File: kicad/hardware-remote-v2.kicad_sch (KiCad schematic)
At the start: 25 parts, among them J1 Flash, J2 TFT, J3 5VIN, J4 3.3VIN, J5 Conn_02x08_Odd_Even, Q1 SI2301CDS-T1-GE3, SW1 ANALOG_LEFT, SW2 ANALOG_RIGHT, U1 ESP32-WROOM-32, U2 AMS1117-3.3

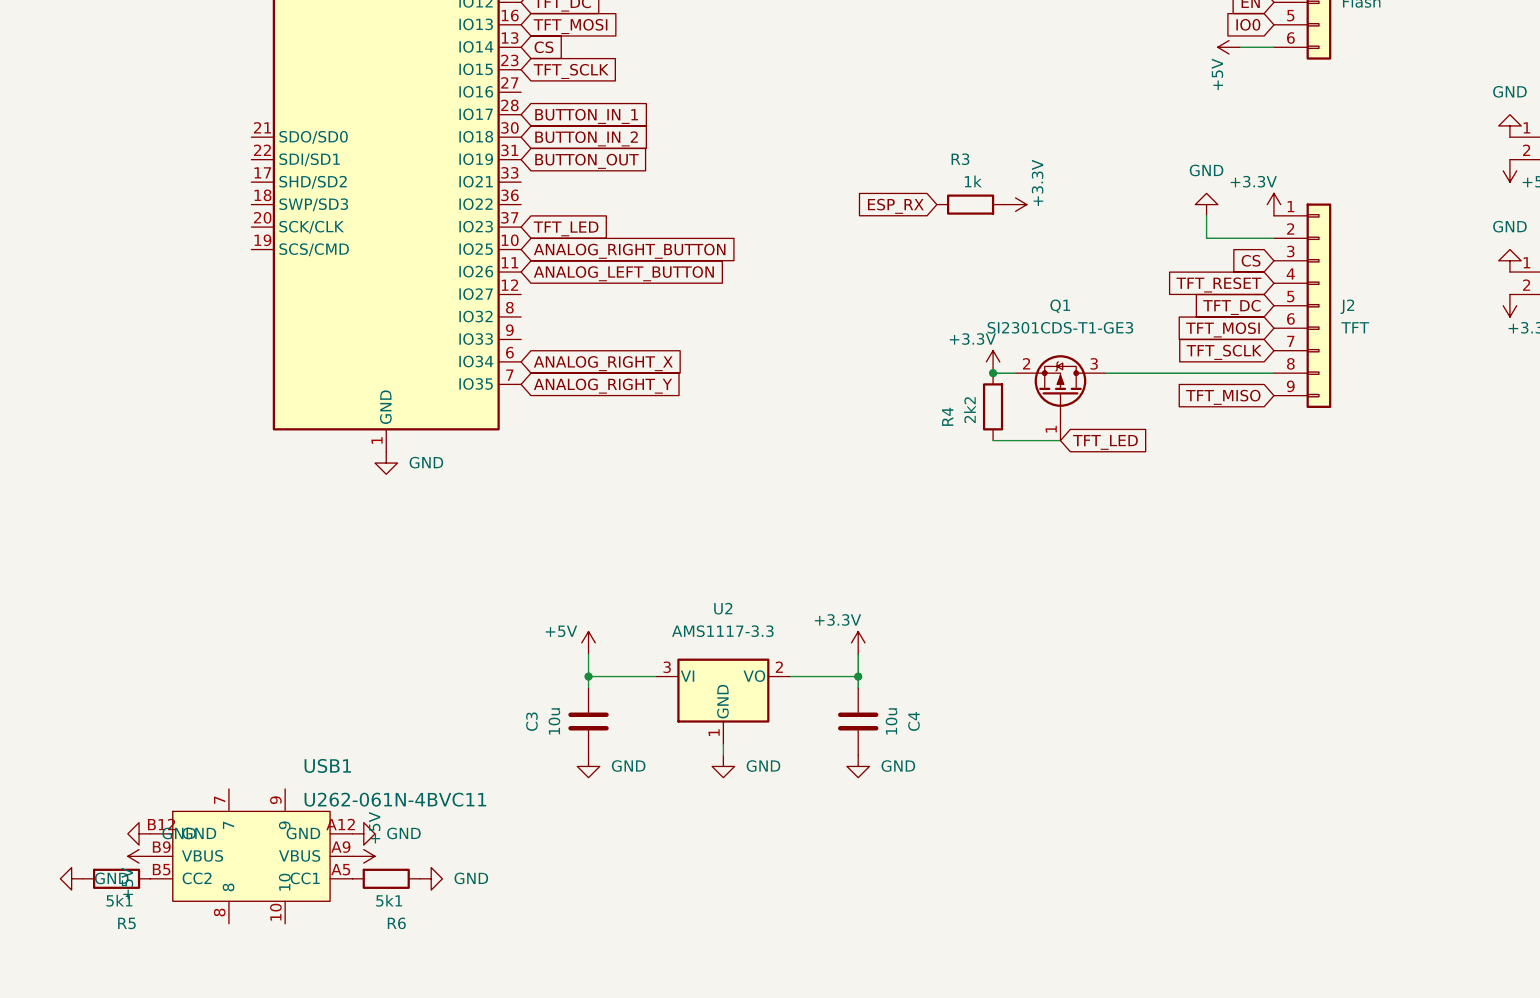
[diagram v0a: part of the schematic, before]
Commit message: Updated usb, still needs someone to put flasher on there
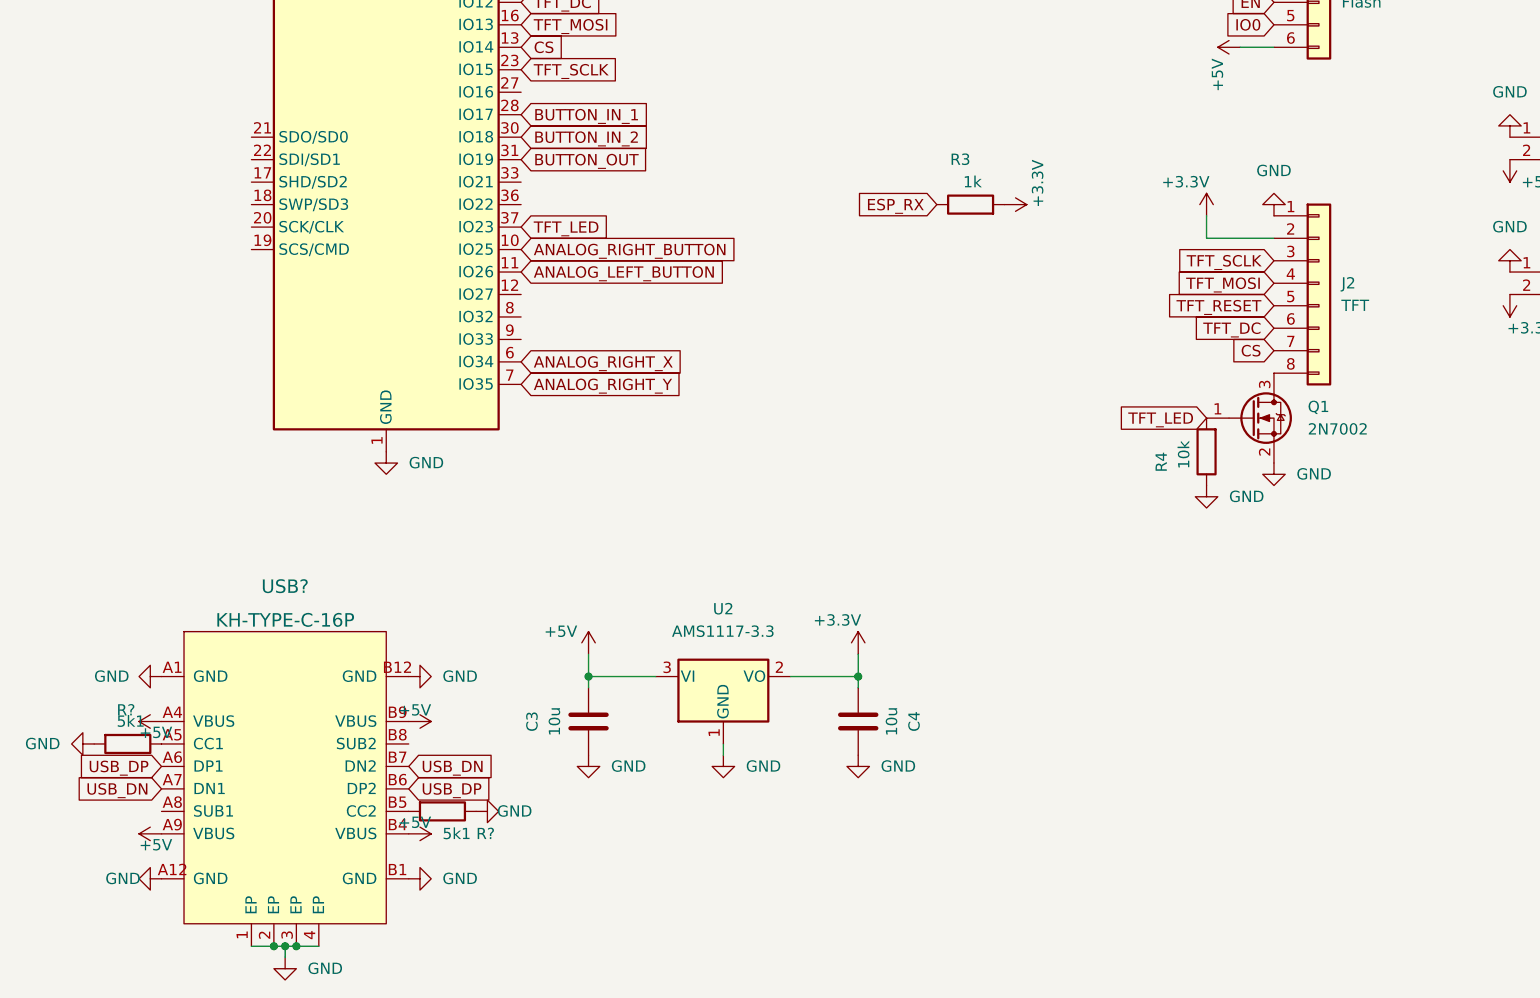
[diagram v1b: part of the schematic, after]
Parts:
- removed Q1: SI2301CDS-T1-GE3, Package_TO_SOT_SMD:SOT-23, symbol Transistor_FET:Si2319CDS
- removed R5, R6: 5k1, Resistor_SMD:R_0603_1608Metric, symbol Device:R
- removed USB1: U262-061N-4BVC11, usb_c_bobby:USB-SMD_U262-061N-4BVC11, symbol usb_c_bobby:U262-061N-4BVC11
- added Q1: 2N7002, Package_TO_SOT_SMD:SOT-23, symbol Transistor_FET:2N7002
- added R? (x2): 5k1, Resistor_SMD:R_0603_1608Metric, symbol Device:R
- added USB?: KH-TYPE-C-16P, usb_c_bobby:USB-C-SMD_KH-TYPE-C-16P, symbol usb_c_bobby:KH-TYPE-C-16P
- J2: footprint Connector_PinSocket_2.54mm:PinSocket_1x09_P2.54mm_Vertical -> Connector_PinSocket_2.54mm:PinSocket_1x08_P2.54mm_Vertical; symbol Connector_Generic:Conn_01x09 -> Connector_Generic:Conn_01x08
- R4: value 2k2 -> 10k; LCSC C4190 -> C25804
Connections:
- net +3V3: now also J2.2 (Pin_2); no longer J2.1 (Pin_1), R4.2
- net +5V: now also USB?.A4 (VBUS), USB?.A9 (VBUS), USB?.B4 (VBUS), USB?.B9 (VBUS)
- net CS: now also J2.7 (Pin_7); no longer J2.3 (Pin_3)
- net GND: now also J2.1 (Pin_1), R4.1, Q1.2 (S), R?.1, R?.2, USB?.1 (EP), USB?.2 (EP), USB?.3 (EP), USB?.4 (EP), USB?.A1 (GND), USB?.A12 (GND), USB?.B1 (GND), USB?.B12 (GND); no longer J2.2 (Pin_2)
- net TFT_DC: now also J2.6 (Pin_6); no longer J2.5 (Pin_5)
- net TFT_LED: now also R4.2, Q1.1 (G); no longer R4.1
- net TFT_MOSI: now also J2.4 (Pin_4); no longer J2.6 (Pin_6)
- net TFT_RESET: now also J2.5 (Pin_5); no longer J2.4 (Pin_4)
- net TFT_SCLK: now also J2.3 (Pin_3); no longer J2.7 (Pin_7)
- net at J2.8 (Pin_8): now also Q1.3 (D)
- removed net TFT_MISO: J2.9 (Pin_9)
- new net: R?.2, USB?.B5 (CC2)
- new net: R?.1, USB?.A5 (CC1)
- new net USB_DN: USB?.A7 (DN1), USB?.B7 (DN2)
- new net USB_DP: USB?.A6 (DP1), USB?.B6 (DP2)
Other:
- moved on the sheet: R4

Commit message: PCB Version Beta 0.1
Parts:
- added C5, C6: 100n, Capacitor_SMD:C_0603_1608Metric, symbol Device:C
- added C7: 1u, Capacitor_SMD:C_0603_1608Metric, symbol Device:C
- added U3: CH343G, Package_SO:SOIC-16_3.9x9.9mm_P1.27mm, symbol wch-usb-uart:CH343G
- R3: value 1k -> 10k; LCSC C21190 -> C25804
- R5, R6: renamed from R?; LCSC C881139 -> C23186
- U1: value ESP32-WROOM-32 -> ESP32-WROOM-32E-8MB; LCSC C82899 -> C701342
- gave numbers to parts that had none: 1
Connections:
- net +3V3: now also C7.2, U3.15 (VIO)
- net +5V: now also C6.2, U3.16 (VDD5), U3.7 (VBUS)
- net EN: now also U3.11 (~{RTS})
- net ESP_RX: now also U3.2 (TXD)
- net ESP_TX: now also U3.3 (RXD)
- net GND: now also C5.1, C6.1, C7.1, U3.1 (GND)
- net IO0: now also U3.10 (~{DTR}/TNOW)
- net USB_DN: now also U3.6 (UD-)
- net USB_DP: now also U3.5 (UD+)
- new net: C5.2, U3.4 (V3)
- no-connect marks 0 -> 5
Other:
- note added: "VDD5"
- note added: "VIO"

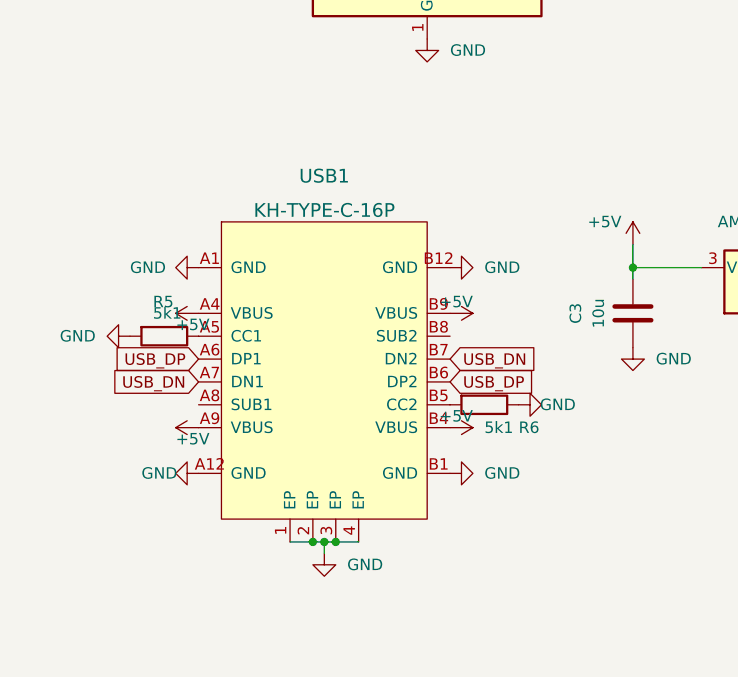
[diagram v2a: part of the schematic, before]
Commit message: Actually use usb c that they can solder
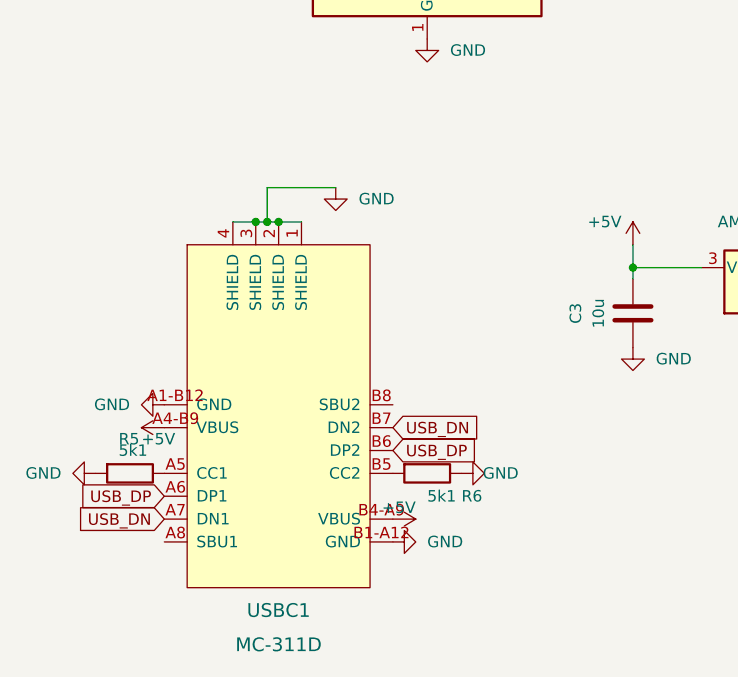
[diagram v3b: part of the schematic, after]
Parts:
- removed USB1: KH-TYPE-C-16P, usb_c_bobby:USB-C-SMD_KH-TYPE-C-16P, symbol usb_c_bobby:KH-TYPE-C-16P
- added USBC1: MC-311D, USB-C-SMD_MC-311D, symbol usb_c_bobby:MC-311D
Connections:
- net +5V: now also USBC1.A4-B9 (VBUS), USBC1.B4-A9 (VBUS)
- net GND: now also USBC1.1 (SHIELD), USBC1.2 (SHIELD), USBC1.3 (SHIELD), USBC1.4 (SHIELD), USBC1.A1-B12 (GND), USBC1.B1-A12 (GND)
- net USB_DN: now also USBC1.A7 (DN1), USBC1.B7 (DN2)
- net USB_DP: now also USBC1.A6 (DP1), USBC1.B6 (DP2)
- net at R6.2: now also USBC1.B5 (CC2)
- net at R5.1: now also USBC1.A5 (CC1)

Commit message: Production files
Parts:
- added C8, C9: 100n, Capacitor_SMD:C_0603_1608Metric, symbol Device:C
- added Q2, Q3: SS8050_C2150, SOT-23-3_L2.9-W1.3-P1.90-LS2.4-BR, symbol SS8050:SS8050_C2150
- added R7, R8: 12k, Resistor_SMD:R_0603_1608Metric, symbol Device:R
- R1: value 47k -> 10k; LCSC C25819 -> C25804
- R2: value 15k -> 10k; LCSC C22809 -> C25804
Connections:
- net +3V3: now also C9.2
- net +5V: now also C8.2
- net EN: now also Q2.3 (C); no longer U3.11 (~{RTS})
- net GND: now also C8.1, C9.1
- net IO0: now also Q3.2 (E); no longer U3.10 (~{DTR}/TNOW)
- new net: Q2.1 (B), R7.2
- new net: Q3.1 (B), R8.2
- new net DTR: Q3.3 (C), R7.1, U3.10 (~{DTR}/TNOW)
- new net RTS: Q2.2 (E), R8.1, U3.11 (~{RTS})

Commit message: Updated / fixed pcb
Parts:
- added R9: 10k, Resistor_SMD:R_0603_1608Metric, symbol Device:R
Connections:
- net GND: now also R9.2
- net TFT_RESET: now also R9.1
- net BUTTON_OUT2: now reaches U1.33 (IO21)
- net BUTTON_OUT2: now also D2.3 (K), D4.3 (K)
- net BUTTON_OUT renamed BUTTON_OUT1
- net BUTTON_OUT1: no longer D2.3 (K), D4.3 (K)
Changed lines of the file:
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@@
   (junction (at 41.91 138.43) (diameter 0) (color 0 0 0 0)
   )
+  (junction (at 110.49 43.18) (diameter 0) (color 0 0 0 0)
+  )
   (junction (at 58.42 43.18) (diameter 0) (color 0 0 0 0)
   )
   (junction (at 58.42 38.1) (diameter 0) (color 0 0 0 0)
   )
-  (junction (at 130.81 38.1) (diameter 0) (color 0 0 0 0)
-  )
-  (junction (at 110.49 38.1) (diameter 0) (color 0 0 0 0)
+  (junction (at 130.81 46.99) (diameter 0) (color 0 0 0 0)
   )
   (junction (at 40.64 138.43) (diameter 0) (color 0 0 0 0)
-  )
-  (junction (at 151.13 38.1) (diameter 0) (color 0 0 0 0)
   )
   (junction (at 74.93 186.69) (diameter 0) (color 0 0 0 0)
@@
     (stroke (width 0) (type default) (color 0 0 0 0))
   )
-  (wire (pts (xy 110.49 38.1) (xy 130.81 38.1))
-    (stroke (width 0) (type default) (color 0 0 0 0))
-  )
   (wire (pts (xy 81.28 143.51) (xy 88.9 143.51))
     (stroke (width 0) (type default) (color 0 0 0 0))
   )
+  (wire (pts (xy 171.45 46.99) (xy 171.45 38.1))
+    (stroke (width 0) (type default) (color 0 0 0 0))
+  )
   (wire (pts (xy 58.42 36.83) (xy 58.42 38.1))
     (stroke (width 0) (type default) (color 0 0 0 0))
@@
     (stroke (width 0) (type default) (color 0 0 0 0))
   )
+  (wire (pts (xy 130.81 46.99) (xy 171.45 46.99))
+    (stroke (width 0) (type default) (color 0 0 0 0))
+  )
   (wire (pts (xy 151.13 91.44) (xy 151.13 93.98))
     (stroke (width 0) (type default) (color 0 0 0 0))
@@
     (stroke (width 0) (type default) (color 0 0 0 0))
   )
+  (wire (pts (xy 130.81 46.99) (xy 130.81 38.1))
+    (stroke (width 0) (type default) (color 0 0 0 0))
+  )
   (wire (pts (xy 82.55 172.72) (xy 88.9 172.72))
     (stroke (width 0) (type default) (color 0 0 0 0))
@@
     (stroke (width 0) (type default) (color 0 0 0 0))
   )
+  (wire (pts (xy 106.68 43.18) (xy 110.49 43.18))
+    (stroke (width 0) (type default) (color 0 0 0 0))
+  )
   (wire (pts (xy 69.85 144.78) (xy 81.28 144.78))
     (stroke (width 0) (type default) (color 0 0 0 0))
   )
-  (wire (pts (xy 130.81 38.1) (xy 151.13 38.1))
+  (wire (pts (xy 106.68 46.99) (xy 130.81 46.99))
     (stroke (width 0) (type default) (color 0 0 0 0))
   )
@@
     (stroke (width 0) (type default) (color 0 0 0 0))
   )
+  (wire (pts (xy 151.13 43.18) (xy 151.13 38.1))
+    (stroke (width 0) (type default) (color 0 0 0 0))
+  )
   (wire (pts (xy 86.36 52.07) (xy 85.09 52.07))
     (stroke (width 0) (type default) (color 0 0 0 0))
   )
-  (wire (pts (xy 107.95 38.1) (xy 110.49 38.1))
+  (wire (pts (xy 110.49 43.18) (xy 151.13 43.18))
     (stroke (width 0) (type default) (color 0 0 0 0))
   )
@@
     (stroke (width 0) (type default) (color 0 0 0 0))
   )
+  (wire (pts (xy 110.49 43.18) (xy 110.49 38.1))
+    (stroke (width 0) (type default) (color 0 0 0 0))
+  )
   (wire (pts (xy 111.76 152.4) (xy 123.19 152.4))
     (stroke (width 0) (type default) (color 0 0 0 0))
@@
   )
   (wire (pts (xy 111.76 140.97) (xy 111.76 143.51))
-    (stroke (width 0) (type default) (color 0 0 0 0))
-  )
-  (wire (pts (xy 151.13 38.1) (xy 171.45 38.1))
     (stroke (width 0) (type default) (color 0 0 0 0))
   )
@@
     )
   )
+  (global_label "BUTTON_OUT2" (shape input) (at 73.66 87.63 0) (fields_autoplaced)
+    (effects (font (size 1.27 1.27)) (justify left))
+    (property "Referenzen zwischen Schaltplänen" "${INTERSHEET_REFS}" (id 0) (at 89.0755 87.5506 0)
+      (effects (font (size 1.27 1.27)) (justify left) hide)
+    )
+  )
   (global_label "ESP_RX" (shape input) (at 158.75 62.23 180) (fields_autoplaced)
     (effects (font (size 1.27 1.27)) (justify right))
@@
     )
   )
-  (global_label "BUTTON_OUT" (shape input) (at 73.66 85.09 0) (fields_autoplaced)
-    (effects (font (size 1.27 1.27)) (justify left))
-    (property "Referenzen zwischen Schaltplänen" "${INTERSHEET_REFS}" (id 0) (at 87.866 85.1694 0)
+  (global_label "BUTTON_OUT1" (shape input) (at 73.66 85.09 0) (fields_autoplaced)
+    (effects (font (size 1.27 1.27)) (justify left))
+    (property "Referenzen zwischen Schaltplänen" "${INTERSHEET_REFS}" (id 0) (at 89.0755 85.0106 0)
       (effects (font (size 1.27 1.27)) (justify left) hide)
     )
@@
     )
   )
-  (global_label "BUTTON_OUT" (shape input) (at 107.95 38.1 180) (fields_autoplaced)
-    (effects (font (size 1.27 1.27)) (justify right))
-    (property "Referenzen zwischen Schaltplänen" "${INTERSHEET_REFS}" (id 0) (at 93.744 38.0206 0)
+  (global_label "BUTTON_OUT1" (shape input) (at 106.68 43.18 180) (fields_autoplaced)
+    (effects (font (size 1.27 1.27)) (justify right))
+    (property "Referenzen zwischen Schaltplänen" "${INTERSHEET_REFS}" (id 0) (at 91.2645 43.1006 0)
       (effects (font (size 1.27 1.27)) (justify right) hide)
     )
@@
     )
   )
+  (global_label "BUTTON_OUT2" (shape input) (at 106.68 46.99 180) (fields_autoplaced)
+    (effects (font (size 1.27 1.27)) (justify right))
+    (property "Referenzen zwischen Schaltplänen" "${INTERSHEET_REFS}" (id 0) (at 91.2645 46.9106 0)
+      (effects (font (size 1.27 1.27)) (justify right) hide)
+    )
+  )
   (global_label "ESP_TX" (shape input) (at 158.75 64.77 180) (fields_autoplaced)
     (effects (font (size 1.27 1.27)) (justify right))
@@
     (effects (font (size 1.27 1.27)) (justify right))
     (property "Referenzen zwischen Schaltplänen" "${INTERSHEET_REFS}" (id 0) (at 182.5231 31.6706 0)
+      (effects (font (size 1.27 1.27)) (justify right) hide)
+    )
+  )
+  (global_label "TFT_RESET" (shape input) (at 120.65 77.47 180) (fields_autoplaced)
+    (effects (font (size 1.27 1.27)) (justify right))
+    (property "Referenzen zwischen Schaltplänen" "${INTERSHEET_REFS}" (id 0) (at 108.5002 77.5494 0)
       (effects (font (size 1.27 1.27)) (justify right) hide)
     )
@@
     )
     (property "Datasheet" "" (id 3) (at 158.75 91.44 0)
+      (effects (font (size 1.27 1.27)) hide)
+    )
+    (pin "1")
+  )
+  (symbol (lib_id "power:GND") (at 128.27 77.47 90) (unit 1)
+    (in_bom yes) (on_board yes)
+    (property "Reference" "#PWR0149" (id 0) (at 134.62 77.47 0)
+      (effects (font (size 1.27 1.27)) hide)
+    )
+    (property "Value" "GND" (id 1) (at 135.89 77.47 90)
+      (effects (font (size 1.27 1.27)) (justify left))
+    )
+    (property "Footprint" "" (id 2) (at 128.27 77.47 0)
+      (effects (font (size 1.27 1.27)) hide)
+    )
+    (property "Datasheet" "" (id 3) (at 128.27 77.47 0)
       (effects (font (size 1.27 1.27)) hide)
     )
@@
     )
     (pin "1")
+  )
+  (symbol (lib_id "Device:R") (at 124.46 77.47 90) (unit 1)
+    (in_bom yes) (on_board yes)
+    (property "Reference" "R9" (id 0) (at 124.46 72.39 90)
+      (effects (font (size 1.27 1.27)) (justify left))
+    )
+    (property "Value" "10k" (id 1) (at 125.73 74.93 90)
+      (effects (font (size 1.27 1.27)) (justify left))
+    )
+    (property "Footprint" "Resistor_SMD:R_0603_1608Metric" (id 2) (at 124.46 79.248 90)
+      (effects (font (size 1.27 1.27)) hide)
+    )
+    (property "Datasheet" "~" (id 3) (at 124.46 77.47 0)
+      (effects (font (size 1.27 1.27)) hide)
+    )
+    (property "LCSC" "C25804" (id 4) (at 124.46 77.47 90)
+      (effects (font (size 1.27 1.27)) hide)
+    )
+    (pin "1")
+    (pin "2")
   )
   (symbol (lib_id "Device:R") (at 38.1 52.07 90) (unit 1)
@@
       (reference "#PWR0148") (unit 1) (value "GND") (footprint "")
     )
+    (path "/2eb2f62e-b835-427a-b1c1-f33b36fee599"
+      (reference "#PWR0149") (unit 1) (value "GND") (footprint "")
+    )
     (path "/6f46814c-caba-4689-a43b-4663914f61cd"
       (reference "#PWR0153") (unit 1) (value "+5V") (footprint "")
@@
       (reference "R8") (unit 1) (value "12k") (footprint "Resistor_SMD:R_0603_1608Metric")
     )
+    (path "/57942a0d-4e6b-4841-bd23-2c78746841a7"
+      (reference "R9") (unit 1) (value "10k") (footprint "Resistor_SMD:R_0603_1608Metric")
+    )
     (path "/a0d604c1-2d87-4f45-a479-8ab155d37b6b"
